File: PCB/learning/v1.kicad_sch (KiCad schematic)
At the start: 8 parts, among them U1 STM32F100C4Tx

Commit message: PCB v0.1: barebones setup
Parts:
- added C8: 1u, symbol Device:C
- added C9: 100n, symbol Device:C
- added FB1: 120R, symbol Device:FerriteBead
- added R1: 10k, symbol Device:R
- added SW1: SW_SPDT, symbol Switch:SW_SPDT
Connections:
- net +3.3V: now also C8.1, FB1.1, SW1.3 (C)
- net +3.3VA: now also FB1.2
- net GND: now also C6.2, C7.2, C8.2, C9.2, SW1.1 (A)
- net BOOT0: now reaches U1.44 (BOOT0)
- net BOOT0: now also R1.2
- net NRST: now reaches U1.7 (NRST)
- net NRST: now also C9.1
- new net SW_BOOT0: R1.1, SW1.2 (B)
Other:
- moved on the sheet: C1, C2, C3, C4, C5

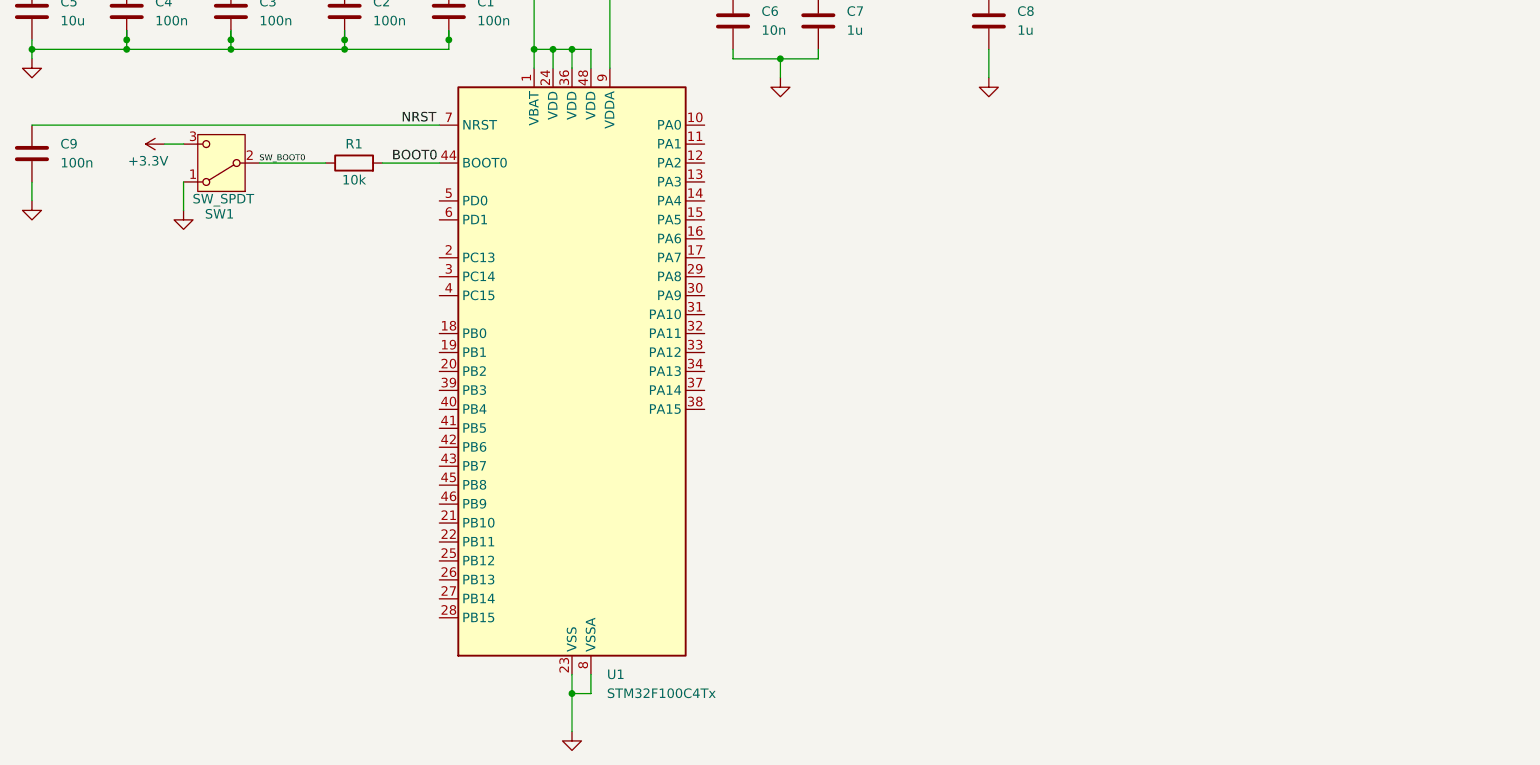
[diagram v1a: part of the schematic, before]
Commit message: add usb-c USB2.0_14P receptacle
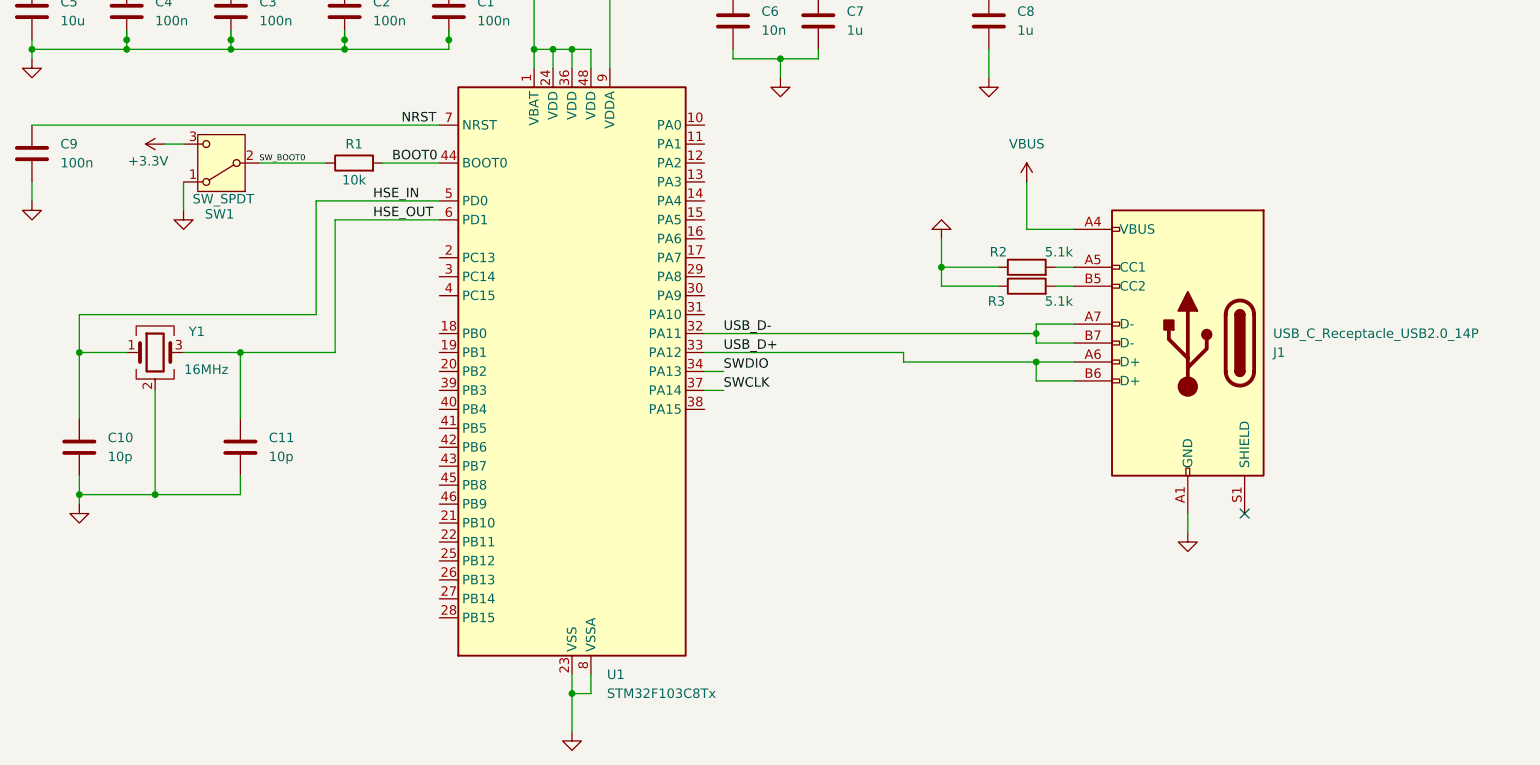
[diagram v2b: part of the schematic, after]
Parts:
- added C10, C11: 10p, symbol Device:C
- added J1: USB_C_Receptacle_USB2.0_14P, symbol Connector:USB_C_Receptacle_USB2.0_14P
- added R2, R3: 5.1k, symbol Device:R
- added Y1: 16MHz, symbol Device:Crystal_GND24
- U1: value STM32F100C4Tx -> STM32F103C8Tx; symbol MCU_ST_STM32F1:STM32F100C4Tx -> MCU_ST_STM32F1:STM32F103C8Tx
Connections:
- net GND: now also C10.2, C11.2, J1.A1 (GND), J1.A12 (GND), J1.B1 (GND), J1.B12 (GND), R2.1, R3.1, Y1.2 (G), Y1.4 (G)
- net USB_D-: now reaches U1.32 (PA11)
- net USB_D-: now also J1.A7 (D-), J1.B7 (D-)
- net USB_D+: now reaches U1.33 (PA12)
- net USB_D+: now also J1.A6 (D+), J1.B6 (D+)
- net SWDIO: now reaches U1.34 (PA13)
- net SWCLK: now reaches U1.37 (PA14)
- net HSE_IN: now reaches U1.5 (PD0)
- net HSE_IN: now also C10.1, Y1.1
- net HSE_OUT: now reaches U1.6 (PD1)
- net HSE_OUT: now also C11.1, Y1.3
- new net: J1.B5 (CC2), R3.2
- new net: J1.A5 (CC1), R2.2
- new net VBUS: J1.A4 (VBUS), J1.A9 (VBUS), J1.B4 (VBUS), J1.B9 (VBUS)
- no-connect marks 0 -> 1

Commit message: STM32F1 series needs pullup resistor for usb-c
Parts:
- added R4: 1.5k, symbol Device:R
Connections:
- net +3.3V: now also R4.2
- net USB_D+: now also R4.1
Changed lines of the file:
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@@
 	)
 	(junction
+		(at 198.12 74.93)
+		(diameter 0)
+		(color 0 0 0 0)
+	)
+	(junction
 		(at 153.67 34.29)
 		(diameter 0)
@@
 	(wire
 		(pts
-			(xy 173.99 74.93) (xy 200.66 74.93)
+			(xy 173.99 74.93) (xy 198.12 74.93)
 		)
 		(stroke
@@
 	(wire
 		(pts
+			(xy 198.12 74.93) (xy 198.12 77.47)
+		)
+		(stroke
+			(width 0)
+			(type default)
+		)
+	)
+	(wire
+		(pts
 			(xy 90.17 83.82) (xy 90.17 74.93)
 		)
@@
 	(wire
 		(pts
+			(xy 198.12 74.93) (xy 200.66 74.93)
+		)
+		(stroke
+			(width 0)
+			(type default)
+		)
+	)
+	(wire
+		(pts
+			(xy 198.12 85.09) (xy 198.12 87.63)
+		)
+		(stroke
+			(width 0)
+			(type default)
+		)
+	)
+	(wire
+		(pts
 			(xy 125.73 22.86) (xy 125.73 25.4)
 		)
@@
 	)
 	(symbol
+		(lib_id "Device:R")
+		(at 198.12 81.28 0)
+		(unit 1)
+		(exclude_from_sim no)
+		(in_bom yes)
+		(on_board yes)
+		(dnp no)
+		(property "Reference" "R4"
+			(at 200.66 80.0099 0)
+			(effects
+				(font
+					(size 1.27 1.27)
+				)
+				(justify left)
+			)
+		)
+		(property "Value" "1.5k"
+			(at 200.66 82.55 0)
+			(effects
+				(font
+					(size 1.27 1.27)
+				)
+				(justify left)
+			)
+		)
+		(property "Footprint" ""
+			(at 196.342 81.28 90)
+			(effects
+				(font
+					(size 1.27 1.27)
+				)
+				(hide yes)
+			)
+		)
+		(property "Datasheet" "~"
+			(at 198.12 81.28 0)
+			(effects
+				(font
+					(size 1.27 1.27)
+				)
+				(hide yes)
+			)
+		)
+		(property "Description" "Resistor"
+			(at 198.12 81.28 0)
+			(effects
+				(font
+					(size 1.27 1.27)
+				)
+				(hide yes)
+			)
+		)
+		(pin "2"
+		)
+		(pin "1"
+		)
+		(instances
+			(project ""
+				(path "/ce74ed80-b7c5-4c1c-b5da-7a9bed7110f1"
+					(reference "R4")
+					(unit 1)
+				)
+			)
+		)
+	)
+	(symbol
 		(lib_id "Device:C")
 		(at 139.7 29.21 0)
@@
 					(unit 1)
 				)
+			)
+		)
+	)
+	(symbol
+		(lib_id "power:+3.3V")
+		(at 198.12 87.63 180)
+		(unit 1)
+		(exclude_from_sim no)
+		(in_bom yes)
+		(on_board yes)
+		(dnp no)
+		(property "Reference" "#PWR015"
+			(at 198.12 83.82 0)
+			(effects
+				(font
+					(size 1.27 1.27)
+				)
+				(hide yes)
+			)
+		)
+		(property "Value" "+3.3V"
+			(at 198.12 91.186 0)
+			(effects
+				(font
+					(size 1.27 1.27)
+				)
+			)
+		)
+		(property "Footprint" ""
+			(at 198.12 87.63 0)
+			(effects
+				(font
+					(size 1.27 1.27)
+				)
+				(hide yes)
+			)
+		)
+		(property "Datasheet" ""
+			(at 198.12 87.63 0)
+			(effects
+				(font
+					(size 1.27 1.27)
+				)
+				(hide yes)
+			)
+		)
+		(property "Description" "Power symbol creates a global label with name \"+3.3V\""
+			(at 198.12 87.63 0)
+			(effects
+				(font
+					(size 1.27 1.27)
+				)
+				(hide yes)
+			)
+		)
+		(pin "1"
+		)
+		(instances
+			(project "v1"
+				(path "/ce74ed80-b7c5-4c1c-b5da-7a9bed7110f1"
+					(reference "#PWR015")
+					(unit 1)
+				)

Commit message: save
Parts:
- added J2: Conn_01x04_Pin, symbol Connector:Conn_01x04_Pin
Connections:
- net USB_D+ is gone; now on net +3.3V: J1.A6 (D+), J1.B6 (D+), R4.1, U1.33 (PA12)
- net +3.3V: now also J2.4 (Pin_4)
- net GND: now also J2.1 (Pin_1)
- net SWCLK: now also J2.2 (Pin_2)
- net SWDIO: now also J2.3 (Pin_3)
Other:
- moved on the sheet: C1, C10, C11, C2, C3, C4, C5, C6, C7, C8, C9, FB1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

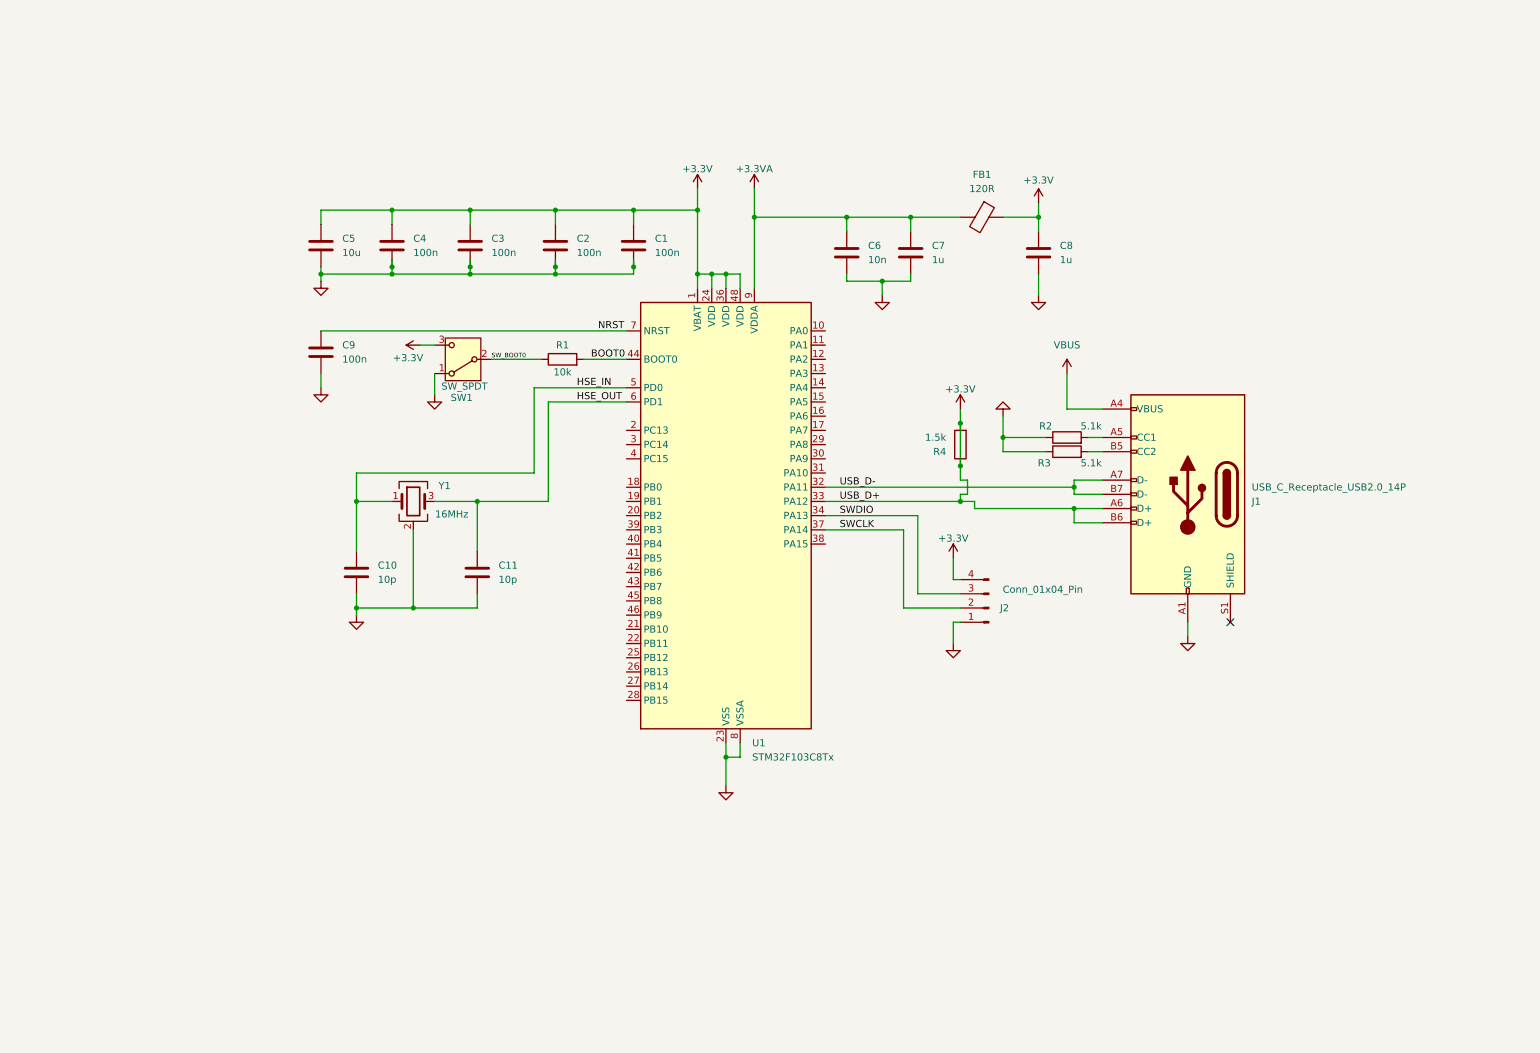
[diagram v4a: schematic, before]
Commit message: init sensors (probably wrong)
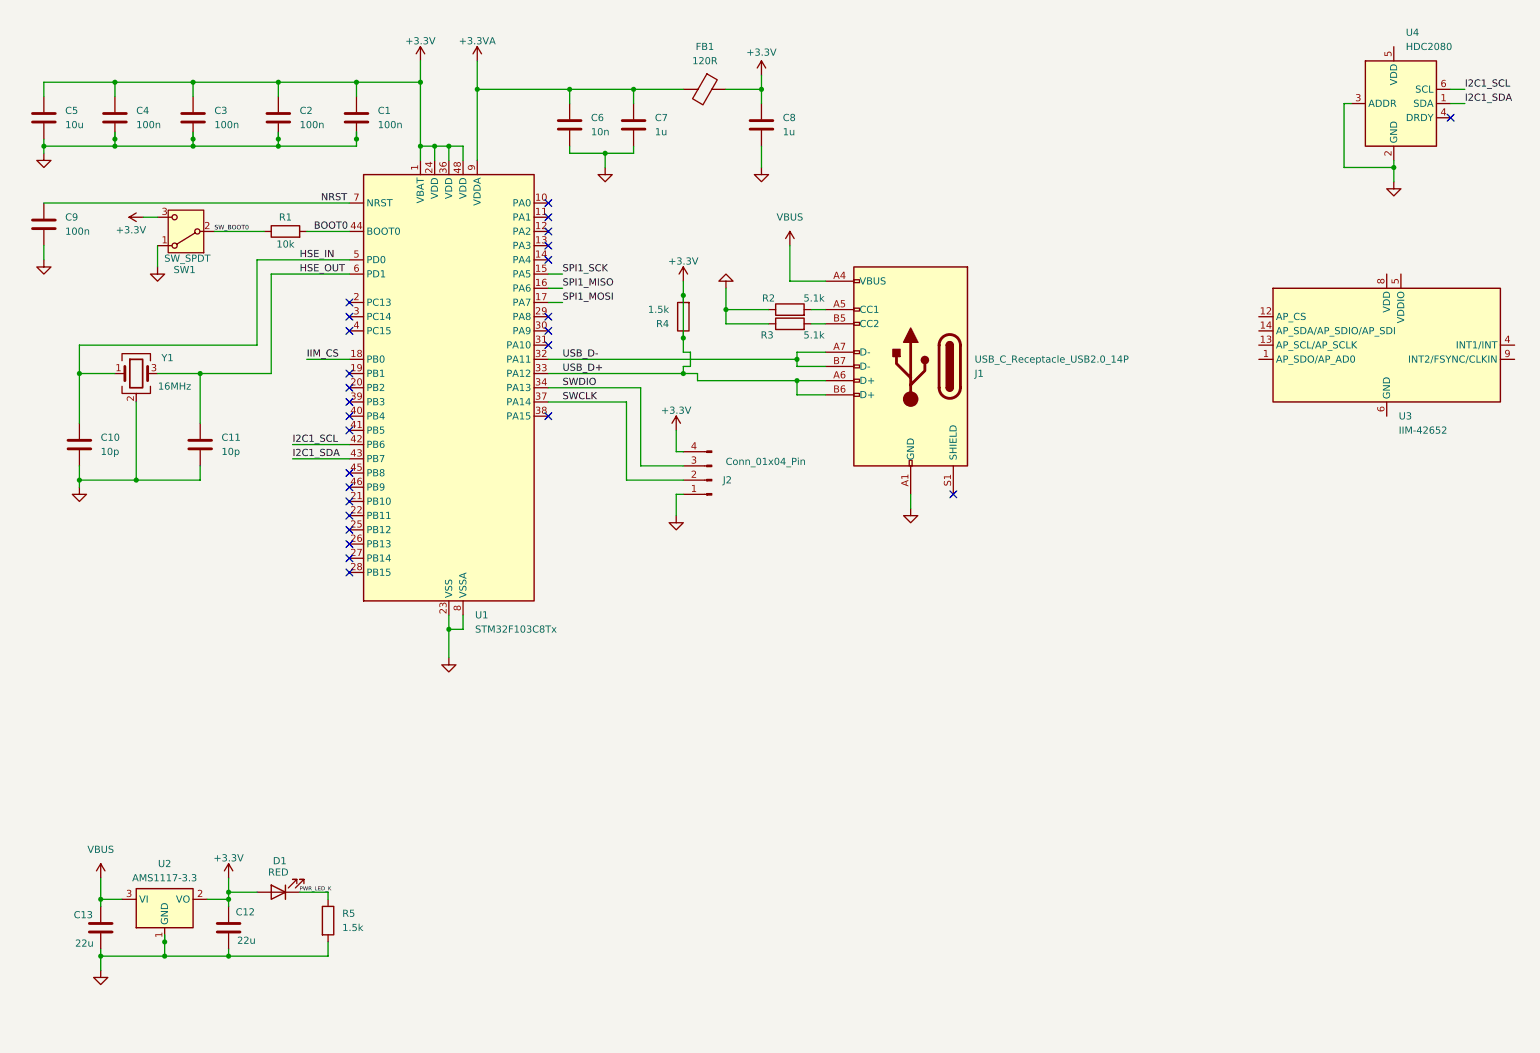
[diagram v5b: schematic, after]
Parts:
- added C12, C13: 22u, symbol Device:C
- added D1: RED, symbol Device:LED
- added R5: 1.5k, symbol Device:R
- added U2: AMS1117-3.3, Package_TO_SOT_SMD:SOT-223-3_TabPin2, symbol Regulator_Linear:AMS1117-3.3
- added U3: IIM-42652, Package_LGA:Bosch_LGA-14_3x2.5mm_P0.5mm, symbol Sensor_Motion:IIM-42652
- added U4: HDC2080, Sensor_Humidity:Texas_S-PWSON-N6-HDC2080, symbol Sensor_Humidity:HDC2080
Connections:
- net +3.3V: now also C12.1, D1.2 (A), U2.2 (VO)
- net GND: now also C12.2, C13.2, R5.2, U2.1 (GND), U4.2 (GND), U4.3 (ADDR)
- net VBUS: now also C13.1, U2.3 (VI)
- net SPI1_SCK: now reaches U1.15 (PA5)
- net SPI1_MISO: now reaches U1.16 (PA6)
- net SPI1_MOSI: now reaches U1.17 (PA7)
- net IIM_CS: now reaches U1.18 (PB0)
- net I2C1_SCL: now reaches U1.42 (PB6)
- net I2C1_SCL: now also U4.6 (SCL)
- net I2C1_SDA: now reaches U1.43 (PB7)
- net I2C1_SDA: now also U4.1 (SDA)
- new net: U3.6 (GND), U3.7 (GND)
- new net PWR_LED_K: D1.1 (K), R5.1
- no-connect marks 1 -> 27
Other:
- moved on the sheet: C1, C10, C11, C2, C3, C4, C5, C6, C7, C8, C9, FB1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

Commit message: add (hopefully) I2C layout for HDC2080
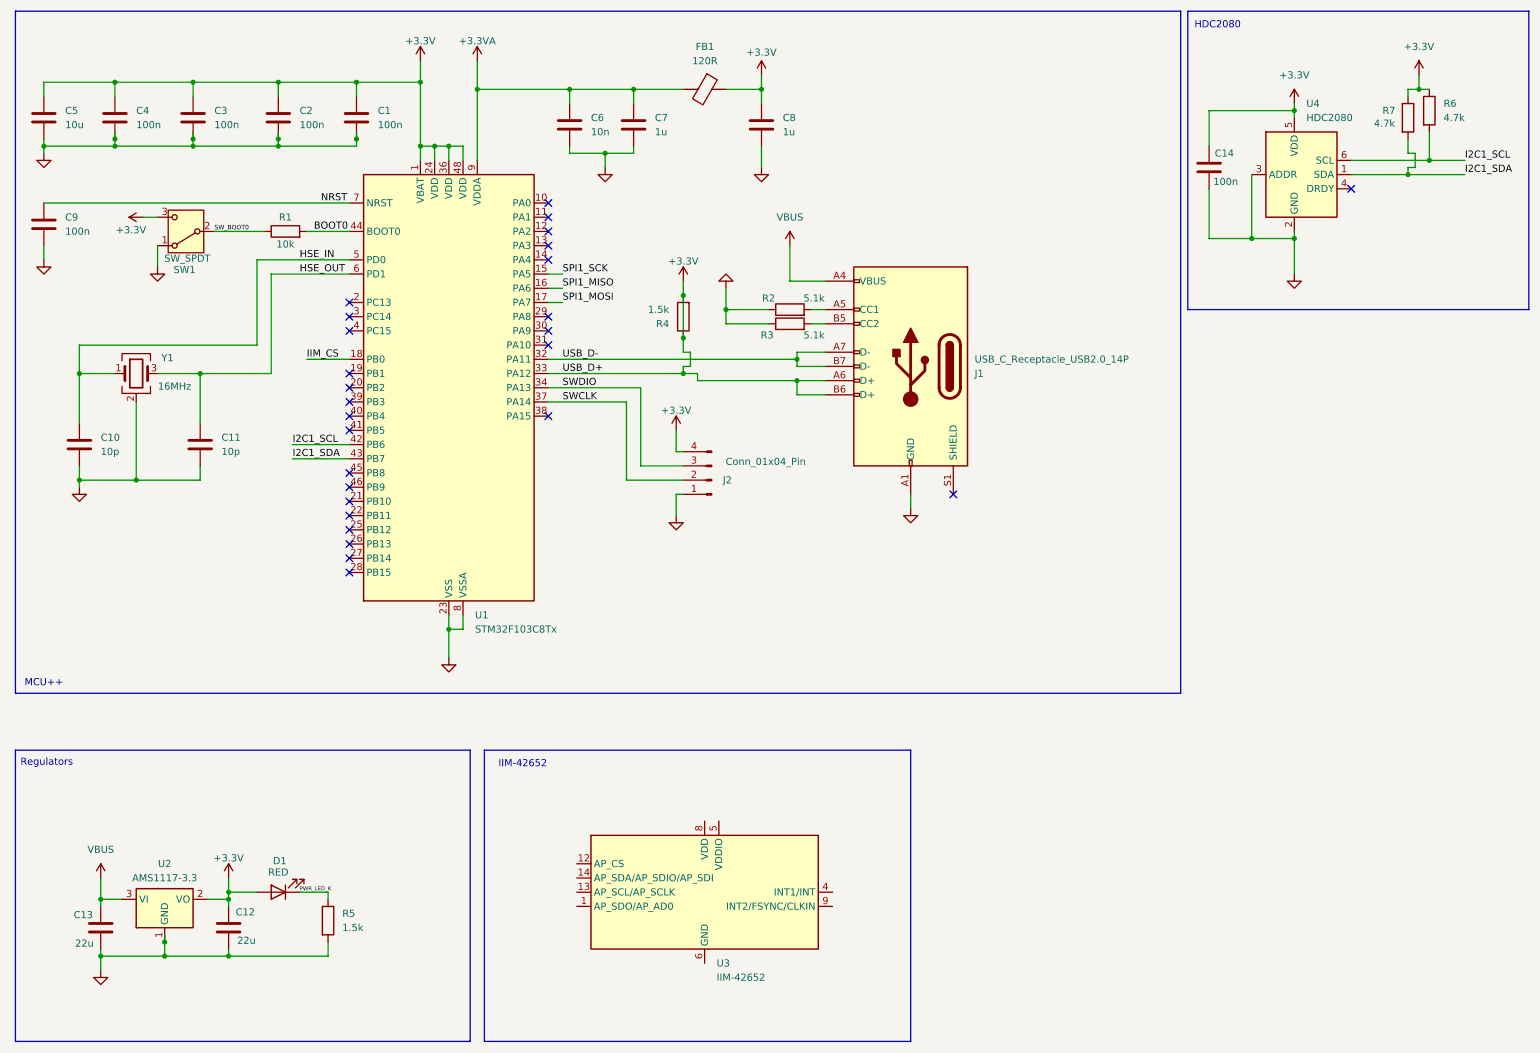
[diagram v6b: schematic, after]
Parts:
- added C14: 100n, symbol Device:C
- added R6, R7: 4.7k, symbol Device:R
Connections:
- net +3.3V: now also U4.5 (VDD), C14.1, R6.1, R7.1
- net GND: now also C14.2
- net I2C1_SCL: now also R6.2
- net I2C1_SDA: now also R7.2
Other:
- note added: "HDC2080"
- note added: "IIM-42652"
- note added: "MCU++"
- note added: "Regulators"
- moved on the sheet: U3, U4
